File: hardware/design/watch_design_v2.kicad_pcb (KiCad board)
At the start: 4 copper layers, 39 x 41.3 mm, 72 parts, among them J1 BAT, J2 USB_C_Receptacle_USB2.0, J3 SWDIO, J4 SWDCLK, J5 ~{RST}, J6 SWO, J7 GND, Q1 BSS138, SW1 SW_Push, SW2 SW_Push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

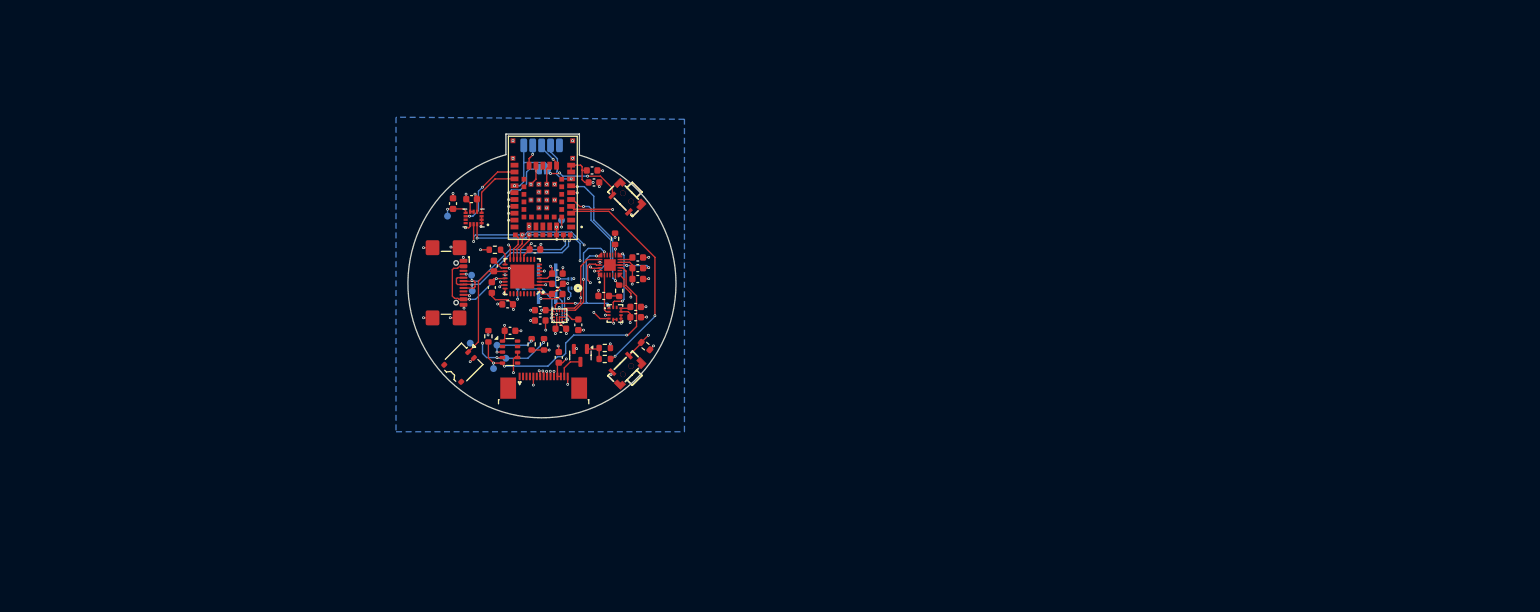
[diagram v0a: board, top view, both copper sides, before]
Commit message: restructured files
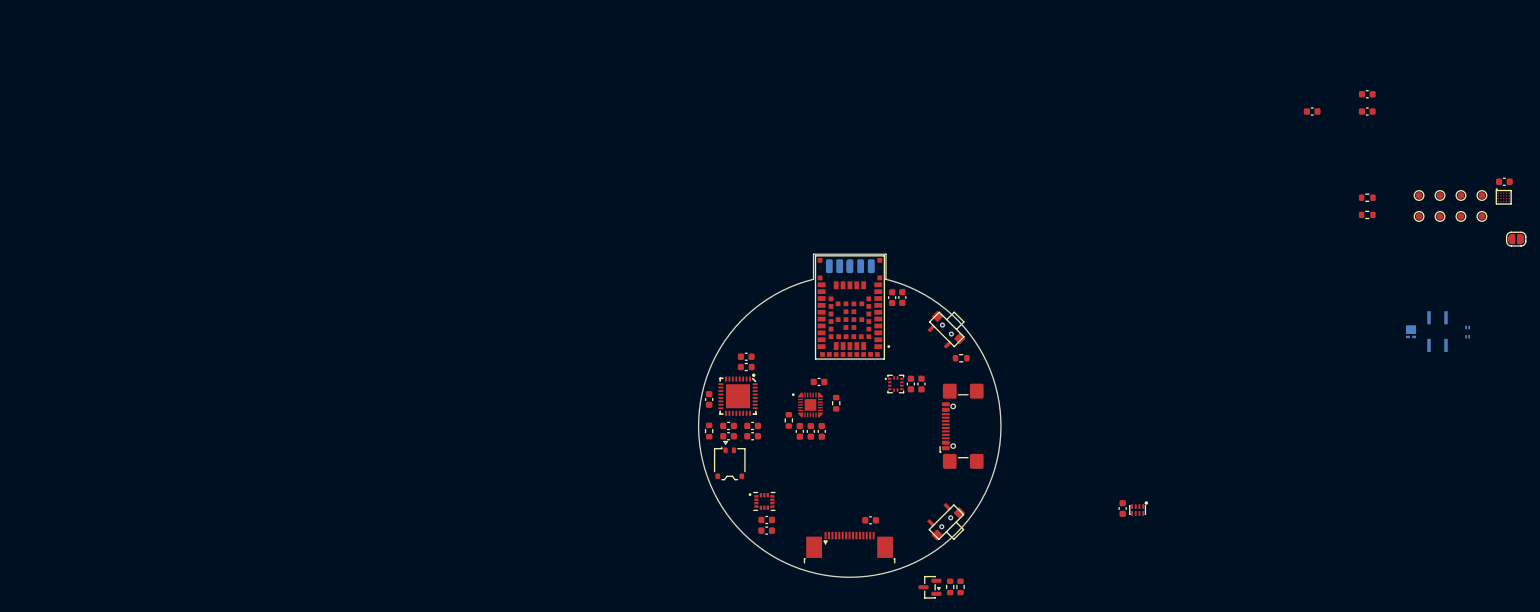
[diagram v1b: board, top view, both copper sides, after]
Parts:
- removed LED2: CT DBLP31.12-6C5D-56-J6Q4, FIREFLY E2218:CT DBLP31.12-6C5D-56-J6Q4_OSR
- removed R11: 4.7k, Resistor_SMD:R_0603_1608Metric
- removed R7: 1k, Resistor_SMD:R_0603_1608Metric
- removed R8: 100n, Resistor_SMD:R_0603_1608Metric
- removed kibuzzard-685D6522: G***, kibuzzard-685D6522
- removed kibuzzard-685D6535: G***, kibuzzard-685D6535
- removed kibuzzard-685D654C: G***, kibuzzard-685D654C
- removed kibuzzard-685D6567: G***, kibuzzard-685D6567
- removed kibuzzard-685D657A: G***, kibuzzard-685D657A
- removed kibuzzard-685D6588: G***, kibuzzard-685D6588
- removed kibuzzard-685D65B1: G***, kibuzzard-685D65B1
- removed kibuzzard-68615877: G***, kibuzzard-68615877
- removed kibuzzard-686159F7: G***, kibuzzard-686159F7
- added LED4: CT DBLP31.12-6C5D-56-J6Q4, FIREFLY E2218:CT DBLP31.12-6C5D-56-J6Q4_OSR, B.Cu at (246.8, 80.3)
- added R2: 47k, Resistor_SMD:R_0603_1608Metric, F.Cu at (144.6, 94.7)
- added R3: 100, Resistor_SMD:R_0603_1608Metric, F.Cu at (156.2, 93.2)
- JP1, TP1, TP2, TP3, TP4, TP5, TP6, TP7, TP8: moved to F.Cu
- R1: value 47k -> 1k
- SW1, SW2: footprint LXTD-0204-034:SW-SMD_LXTD-0204-034 -> OSW:button_side_smd
- U2: value SFH_7015 -> SFH 7015; footprint SFH-7015:SFH 7015_OSR -> SFH-7015:SFH7015
- U3: value RV-8523-C3 -> RV-8263-C8 32.768KHZ 20PPM TA QA; footprint Package_SON:RTC_SMD_MicroCrystal_C3_2.5x3.7mm -> rv8263-c8:OSC-SMD_8P-L2.0-W1.2
- moved TP8 148.5 mm to (257.1, 63.5), turned to 0 degrees
- moved TP5 147.6 mm to (254.1, 60.4)
- moved TP6 142.6 mm to (254.1, 63.5), turned to 0 degrees
- moved JP1 142.1 mm to (262.1, 66.8)
- moved C13 141.6 mm to (260.4, 58.4), turned to 0 degrees
- moved TP3 141.5 mm to (251.0, 60.4), turned to 0 degrees
- moved TP4 141.3 mm to (251.0, 63.5), turned to 0 degrees
- moved U1 138.6 mm to (260.3, 60.7)
- moved TP2 135.6 mm to (248.0, 63.5), turned to 0 degrees
- moved TP1 135.1 mm to (248.0, 60.4), turned to 0 degrees
- moved TP7 134.1 mm to (257.1, 60.4), turned to 0 degrees
- moved U2 130.6 mm to (255.0, 80.3), turned to 90 degrees
- moved LED3 129.8 mm to (250.7, 82.2)
- moved LED1 129.8 mm to (250.7, 78.2)
- moved R5 123.1 mm to (240.4, 63.2), turned to 0 degrees
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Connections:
- C6 pad 1: VUSB -> VDD
- J1 pad 1: +BATT -> GND
- J1 pad 2: GND -> +BATT
- R1 pad 1: /VSET1 -> +1V8
- R1 pad 2: GND -> BTN1
- R6 pad 2: SQW -> ~{PPG_INT}
- U3 pad 1: +1V8 -> SDA
- U3 pad 2: unconnected-(U3-~{INT_1}-Pad2) -> CLKOE
- U3 pad 3: SCL -> unconnected-(U3-~{INT}-Pad3)
- U3 pad 4: SDA -> GND
- U3 pad 5: SQW -> +1V8
- U3 pad 7: GND -> SQW
- U3 pad 8: GND -> SCL
- U5 pad 21: VUSB -> VDD
- U6 pad 17: MEM_INT2 -> MEM_INT1
- U6 pad 18: MEM_INT1 -> MEM_INT2
- U6 pad 20: ~{TFT_RST} -> CLKOE
- U8 pad 5: GND -> unconnected-(U8-NC-Pad5)
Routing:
- net GND: track 76.3 -> 0.00 mm, vias 64 -> 0
- net SDA: track 56.6 -> 0.00 mm, vias 7 -> 0
- net SCL: track 55.8 -> 0.00 mm, vias 6 -> 0
- net +1V8: track 45.3 -> 0.00 mm, vias 15 -> 0
- net ~{TFT_RST}: track 41.3 -> 0.00 mm, vias 2 -> 0
- net SQW: track 38.4 -> 0.00 mm, vias 3 -> 0
- net TFT_MOSI: track 33.4 -> 0.00 mm, vias 2 -> 0
- net TFT_BCKL: track 32.7 -> 0.00 mm, vias 2 -> 0
- net TFT_SCK: track 32.3 -> 0.00 mm, vias 2 -> 0
- net BTN1: track 32.0 -> 0.00 mm, vias 2 -> 0
- net ~{TFT_CS}: track 31.1 -> 0.00 mm, vias 2 -> 0
- net TFT_DC: track 29.8 -> 0.00 mm, vias 2 -> 0
- net D-: track 23.2 -> 0.00 mm, vias 2 -> 0
- net VBUS: track 23.0 -> 0.00 mm, vias 3 -> 0
- net ~{RST}: track 23.0 -> 0.00 mm, vias 4 -> 0
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- removed copper zone on In2.Cu, net +1V8
- removed copper zone on B.Cu, net GND
- removed copper zone on In1.Cu, net VCC
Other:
- board size 39 x 41.3 mm -> 44 x 47 mm

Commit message: updated design as a two part pcb
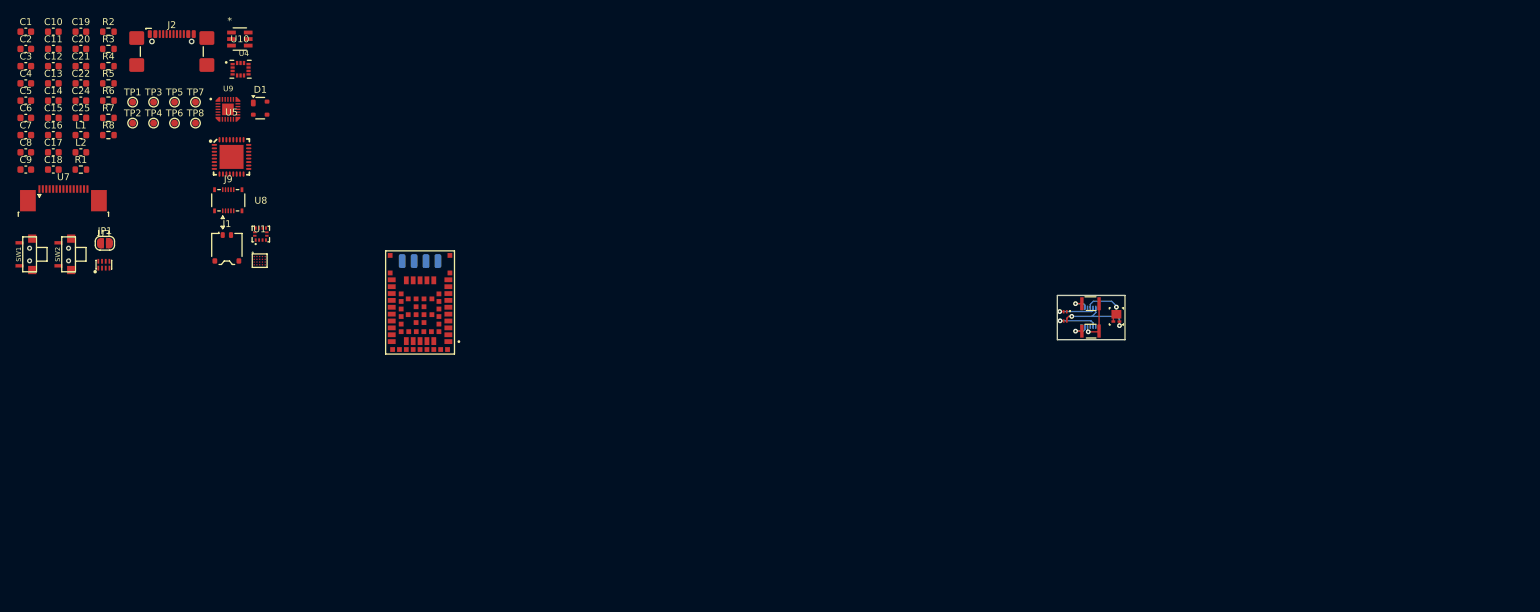
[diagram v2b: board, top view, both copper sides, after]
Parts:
- removed J5: ~{RST}, Connector_Wire:SolderWirePad_1x01_SMD_1x2mm
- removed Q1: BSS138, Package_TO_SOT_SMD:SOT-23
- removed R10: 470, Resistor_SMD:R_0603_1608Metric
- removed R9: 47k, Resistor_SMD:R_0603_1608Metric
- added C16: 100n, Capacitor_SMD:C_0603_1608Metric, F.Cu at (49.1, 51.6)
- added C17: 10u, Capacitor_SMD:C_0603_1608Metric, F.Cu at (49.1, 54.1)
- added D1: PRTR5V0U2X, Package_TO_SOT_SMD:SOT-143, F.Cu at (79.2, 47.7)
- added J8: HRM_M, Connector_Hirose_DF40:Hirose_DF40C-10DP-0.4V_2x05-1MP_P0.4mm, B.Cu at (200.1, 78.1)
- added J9: HRM_F, Connector_Hirose_DF40:Hirose_DF40B-10DS-0.4V_2x05-1MP_P0.4mm, F.Cu at (74.6, 61.1)
- added L2: 2.2uH, Inductor_SMD:L_0603_1608Metric, F.Cu at (53.1, 54.1)
- added R7: 56.2k, Resistor_SMD:R_0603_1608Metric, F.Cu at (57.1, 49.1)
- added R8: 150k, Resistor_SMD:R_0603_1608Metric, F.Cu at (57.1, 51.6)
- added U10: FAN5622SX, FAN5622:SSOT6_3X1P7_ONS, F.Cu at (76.3, 37.6)
- LED1, LED3, LED4, U2: moved to F.Cu
- moved C13 211.8 mm to (49.1, 44.1)
- moved JP1 205.5 mm to (56.6, 67.4)
- moved TP1 187.8 mm to (60.6, 46.8)
- moved TP2 187.8 mm to (60.6, 49.9)
- moved TP3 187.8 mm to (63.7, 46.8)
- moved TP4 187.8 mm to (63.7, 49.9)
- moved TP5 187.8 mm to (66.7, 46.8)
- moved TP6 187.8 mm to (66.7, 49.9)
- moved TP7 187.8 mm to (69.8, 46.8)
- moved TP8 187.8 mm to (69.8, 49.9)
- moved C2 187.5 mm to (45.1, 39.1)
- moved C21 187.4 mm to (53.1, 41.6)
- moved C22 187.4 mm to (53.1, 44.1)
- moved R4 184.3 mm to (57.1, 41.6)
- moved R5 184.3 mm to (57.1, 44.1)
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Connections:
- net /SW1 renamed /main_board/SW1
- net /VCORE renamed /main_board/VCORE
- net /VREF renamed /main_board/VREF
- net /VSET1 renamed /main_board/VSET1
- net /~{MAX_RST_0} renamed /main_board/~{MAX_RST_0}
- C10 pad 2: VCC -> +3V0
- C6 pad 1: VDD -> VUSB
- J2 pad A4: VUSB -> VBUS
- J2 pad A9: VUSB -> VBUS
- J2 pad B4: VUSB -> VBUS
- J2 pad B9: VUSB -> VBUS
- LED1 pad 1: /PD1 -> /PPG/PD1_Q
- LED1 pad 2: GND -> GND1
- LED3 pad 1: /PD2 -> /PPG/PD2_Q
- LED3 pad 2: GND -> GND1
- LED4 pad 1: /GREEN -> /PPG/GREEB_Q
- LED4 pad 2: VCC -> VCCQ
- LED4 pad 3: /GREEN -> /PPG/GREEB_Q
- U1 pad A1: VCC -> +3V0
- U1 pad B1: /GREEN -> GREEN
- U1 pad C1: /IR -> IR
- U1 pad D1: /RED -> RED
- U1 pad D4: /PD2 -> PD2
- U1 pad D5: /PD1 -> PD1
- U2 pad 2: /RED -> /PPG/RED_Q
- U2 pad 3: VCC -> VCCQ
- U2 pad 4: /IR -> /PPG/IR_Q
- U5 pad 12: VCC -> +1V8
- U5 pad 16: GND -> /main_board/VSET2
- U5 pad 21: VDD -> VBUS
- U5 pad 22: VBUS -> VUSB
- U5 pad 32: unconnected-(U5-VOUT2-Pad32) -> +3V0
- U5 pad 5: unconnected-(U5-SW2-Pad5) -> Net-(U5-SW2)
- U6 pad 31: VBUS -> VUSB
- U7 pad 2: /LEDK -> /main_board/LEDK
- U7 pad 3: VCC -> +3V0
- U7 pad 4: VCC -> +3V0
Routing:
- net VCCQ: track 0.00 -> 11.3 mm, vias 0 -> 2
- net /PPG/GREEB_Q: track 0.00 -> 7.23 mm, vias 0 -> 1
- net GND1: track 0.00 -> 6.43 mm, vias 0 -> 1
- net /PPG/IR_Q: track 0.00 -> 5.99 mm, vias 0 -> 1
- net /PPG/RED_Q: track 0.00 -> 5.85 mm, vias 0 -> 1
- net /PPG/PD1_Q: track 0.00 -> 2.81 mm, vias 0 -> 1
- net /PPG/PD2_Q: track 0.00 -> 2.78 mm, vias 0 -> 1
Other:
- board size 44 x 47 mm -> 9.8 x 6.5 mm

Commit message: updated design to include two boards connected back to back
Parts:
- added C23: 100n, Capacitor_SMD:C_0603_1608Metric, F.Cu at (93.7, 83.5)
- added C26: 100n, Capacitor_SMD:C_0603_1608Metric, F.Cu at (93.7, 89.1)
- D1, J9, JP1, TP3, U7: moved to B.Cu
- SW1, SW2: footprint OSW:button_side_smd -> Button_Switch_SMD:SW_SPST_B3U-3000P-B
- moved R2 90.4 mm to (126.7, 94.2)
- moved C5 87.2 mm to (124.1, 83.5), turned to -90 degrees
- moved C6 85.3 mm to (118.7, 92.3), turned to -90 degrees
- moved C1 84.7 mm to (110.1, 90.8), turned to 90 degrees
- moved C3 83.8 mm to (118.8, 81.4), turned to 180 degrees
- moved C10 83.2 mm to (99.5, 102.7)
- moved R8 80.7 mm to (126.7, 92.5)
- moved C14 80.6 mm to (115.5, 92.3), turned to -90 degrees
- moved C15 80.6 mm to (117.1, 92.3), turned to -90 degrees
- moved C20 79.1 mm to (106.2, 97.7)
- moved C2 76.8 mm to (105.5, 86.5)
- moved C9 76.1 mm to (112.3, 92.3), turned to -90 degrees
- moved C19 75.8 mm to (106.4, 90.5)
- moved R3 75.1 mm to (109.2, 93.2)
- moved LED4 73.2 mm to (130.8, 81.4), turned to -90 degrees
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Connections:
- net Net-(U10-ISET) renamed /main_board/ISET
- net Net-(U5-SW2) renamed /main_board/SW2
- C13 pad 1: VCC -> +3V0
- C17 pad 1: +3.3V -> +3V0
- D1 pad 2: D- -> D+
- D1 pad 3: D+ -> D-
- L2 pad 1: +3.3V -> +3V0
- U6 pad 21: TFT_MOSI -> TFT_DC
- U6 pad 22: TFT_SCK -> ~{TFT_CS}
- U6 pad 23: ~{TFT_CS} -> TFT_SCK
- U6 pad 24: TFT_DC -> TFT_MOSI
- U6 pad 48: SCL -> SDA
- U6 pad 49: SDA -> SCL
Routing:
- net TFT_DC: track 0.00 -> 42.2 mm, vias 0 -> 1
- net ~{TFT_CS}: track 0.00 -> 42.1 mm, vias 0 -> 1
- net TFT_SCK: track 0.00 -> 41.5 mm, vias 0 -> 1
- net TFT_MOSI: track 0.00 -> 40.8 mm, vias 0 -> 1
- net ~{TFT_RST}: track 0.00 -> 34.7 mm
- net CLKOE: track 0.00 -> 29.0 mm, vias 0 -> 2
- net SDA: track 0.00 -> 25.7 mm
- net SCL: track 0.00 -> 24.8 mm, vias 0 -> 2
- net GND: track 0.00 -> 24.1 mm, vias 0 -> 47
- net MFIO: track 0.00 -> 23.8 mm
- net SCK: track 0.00 -> 22.7 mm, vias 0 -> 2
- net ACCEL_INT: track 0.00 -> 19.6 mm, vias 0 -> 2
- net D-: track 0.00 -> 19.2 mm, vias 0 -> 2
- net D+: track 0.00 -> 18.3 mm, vias 0 -> 2
- net ACCEL_CS: track 0.00 -> 17.2 mm, vias 0 -> 2
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- added copper zone on F.Cu, net +1V8
- added copper zone on F.Cu, net +3V0
- added copper zone on B.Cu, net GND
- added copper zone on B.Cu, net GND1
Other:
- board size 9.8 x 6.5 mm -> 55.9 x 39.8 mm
- copper layers 4 -> 2
